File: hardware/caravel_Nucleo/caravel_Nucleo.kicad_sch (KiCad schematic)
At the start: 82 parts, among them J1 USB4105-GF-A, J10 PinHeader_1x11, J11 PinHeader_1x02, J12 PinHeader_1x02, J3 PinHeader_1x02, J4 836-22-004-10-001101, J5 PinHeader_1x02, J6 PinHeader_1x02, J7 836-22-006-10-001101, J8 640456-3, J9 640456-3, SW1 KMR2, T1 Logo, T2 Logo, U1 FT232HQ, U12 NUCLEO144-F429ZI, U2 SN74LVC1G125DCKR, U3 SN74LVC1G125DCKR, U4 MAX811REUS+T, U7 W25Q32FVSS, U8 caravel_breakout, U9 MIC2211-AAYML-TR, X1 ECS-2520MVLC-100-BN-TR, Y1 ABM8G-12.000MHZ-18-D2Y-T

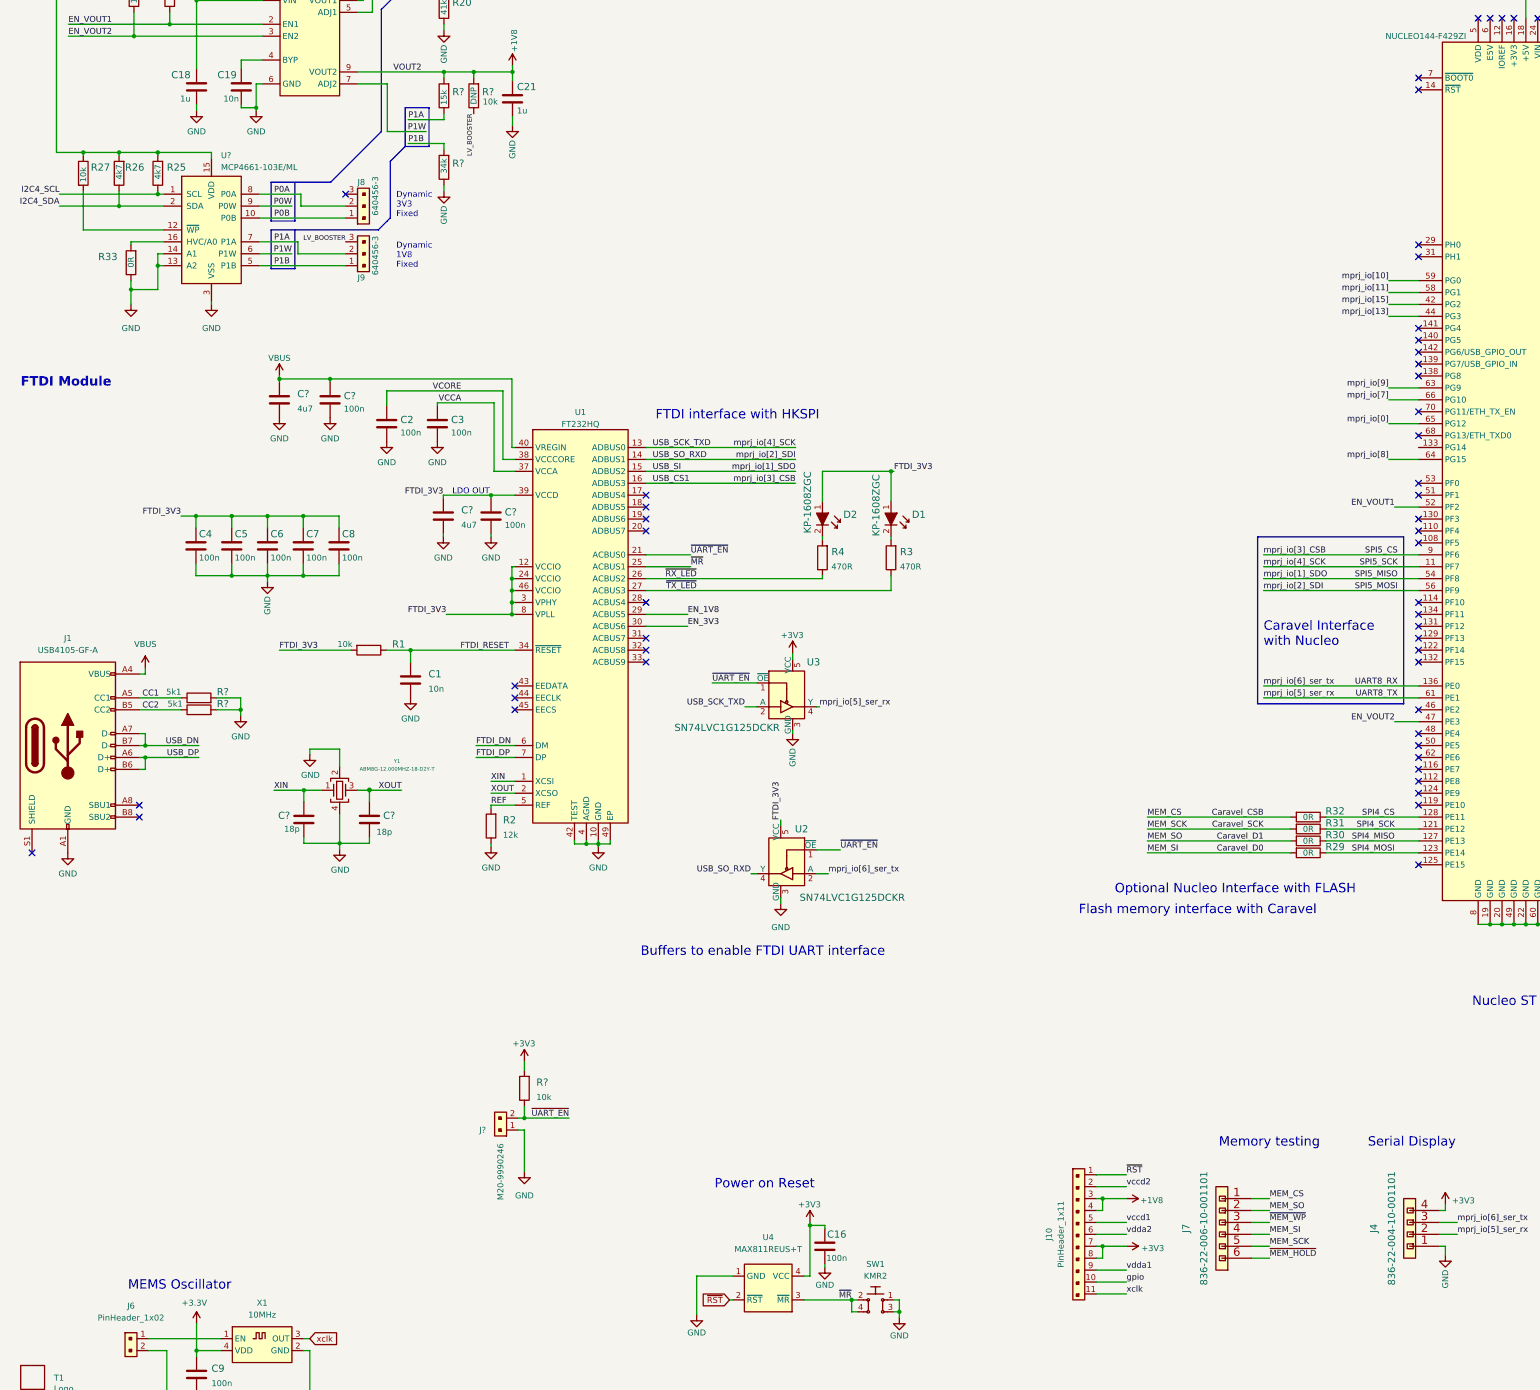
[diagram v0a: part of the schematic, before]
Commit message: Annotate parts on schematic
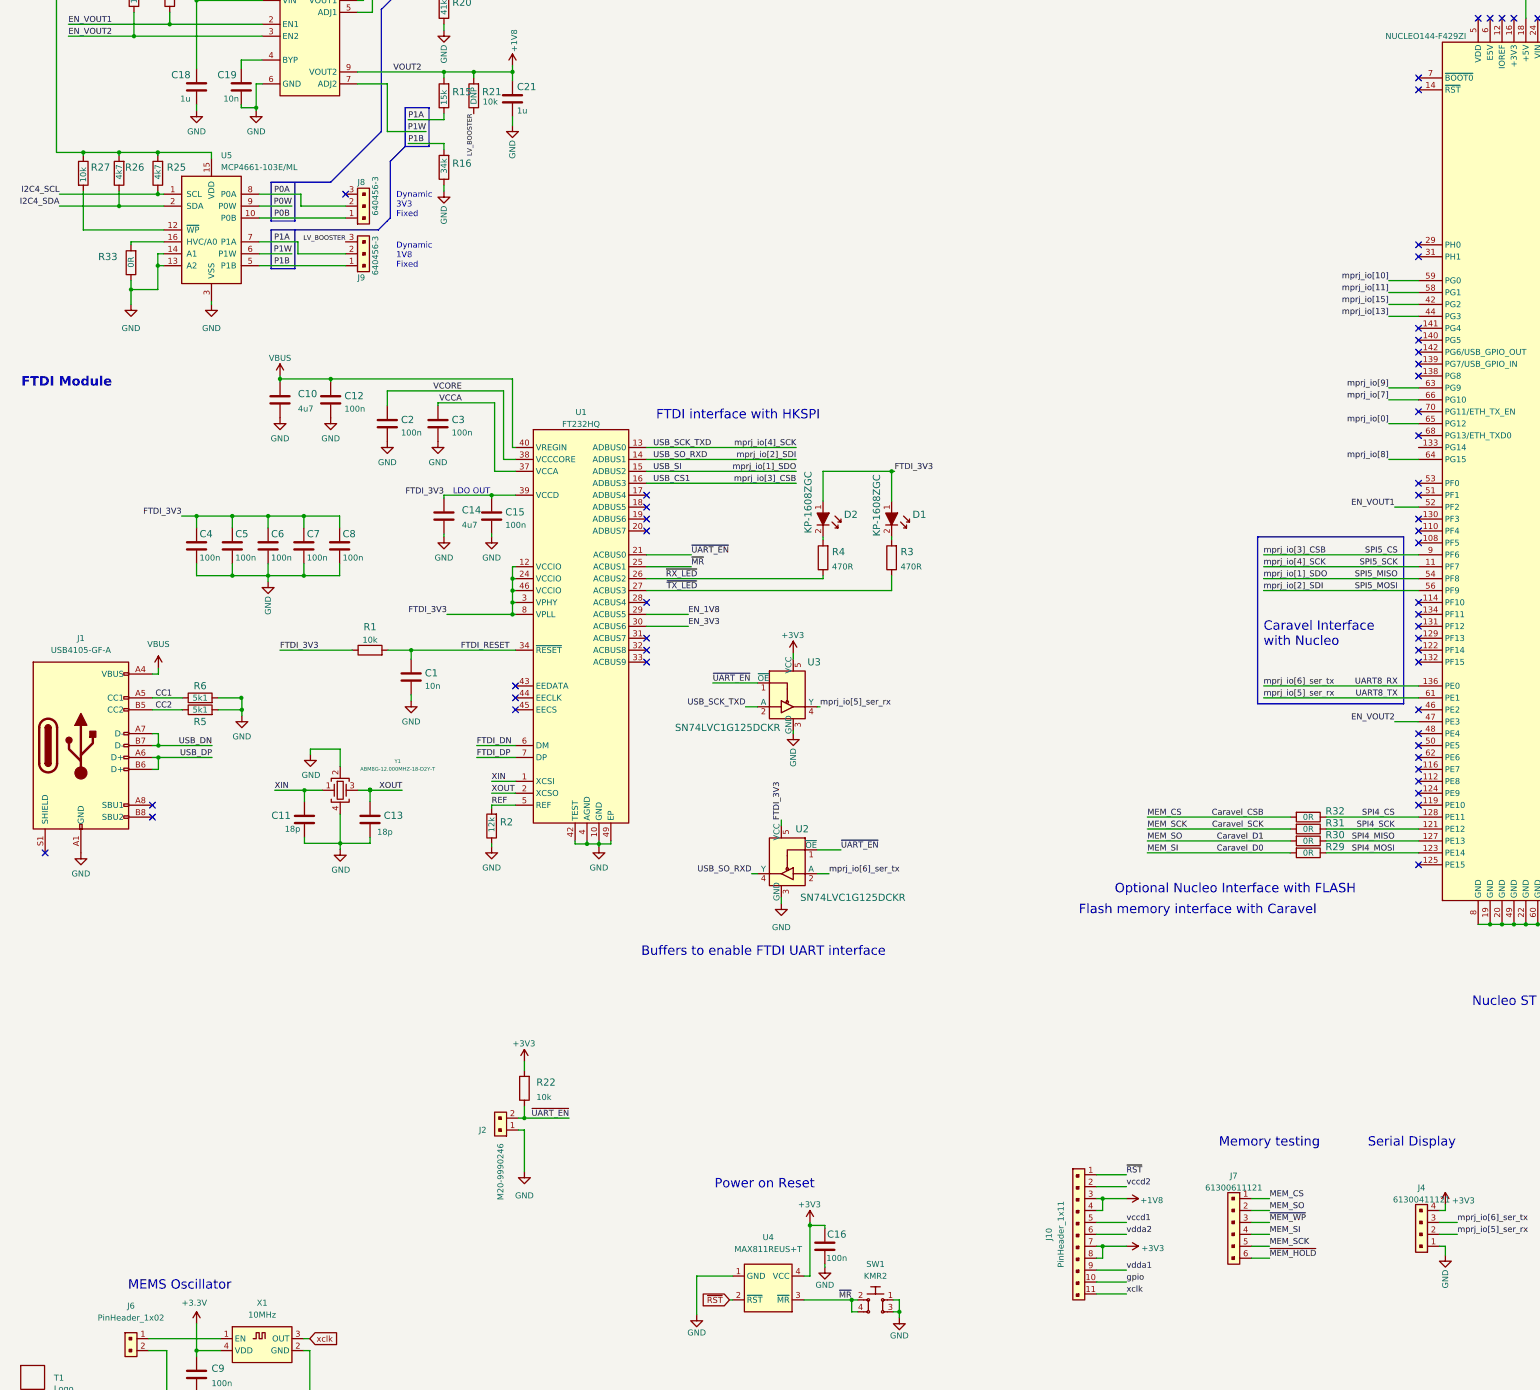
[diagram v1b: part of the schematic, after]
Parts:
- removed C1: C_10n_0402, antmicro-footprints:0402-cap, symbol antmicroCapacitors0402:C_10n_0402
- removed J4: 836-22-004-10-001101, antmicro-footprints:PogoPinHeader_1x4_P2mm_Drill1,5mm, symbol antmicroRectangularConnectorsHeadersMalePins:836-22-004-10-001101
- removed J7: 836-22-006-10-001101, antmicro-footprints:PogoPinHeader_1x6_P2mm_Drill1,5mm, symbol antmicroRectangularConnectorsHeadersMalePins:836-22-006-10-001101
- removed R1: R_10k_0402, antmicro-footprints:0402-res, symbol antmicroResistors0402:R_10k_0402
- removed R2: R_12k_0402, antmicro-footprints:0402-res, symbol antmicroResistors0402:R_12k_0402
- removed R? (x2): R_5k1_0402, antmicro-footprints:0402-res, symbol antmicroResistors0402:R_5k1_0402
- added C1: C_10n_0603, antmicro-footprints:0603-cap, symbol antmicroCapacitors0603:C_10n_0603
- added J4: 61300411121, antmicro-footprints:PinHeader_1x4_P2.54mm_Drill1.02mm, symbol antmicroRectangularConnectorsHeadersMalePins:61300411121
- added J7: 61300611121, antmicro-footprints:61300611121, symbol antmicroRectangularConnectorsHeadersMalePins:61300611121
- added R1: R_10k_0603, antmicro-footprints:0603-res, symbol antmicroResistors0603:R_10k_0603
- added R2: R_12k_0603, antmicro-footprints:0603-res, symbol antmicroResistors0603:R_12k_0603
- added R5, R6: R_5k1_0603, antmicro-footprints:0603-res, symbol antmicroResistors0603:R_5k1_0603
- T1: footprint Caravel_Board:logo -> antmicro-footprints:efabless_logo_2
- T2: footprint Caravel_Board:ef_logo -> antmicro-footprints:efabless_logo
- gave numbers to parts that had none: 12
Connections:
- net +3V3: now also J4.4
- net AGND: now also C1.2, J4.1, R2.1, R5.2, R6.2
- net CC1: now also R6.1
- net CC2: now also R5.1
- net Caravel_CSB: now also J7.1
- net Caravel_D0: now also J7.4
- net Caravel_D1: now also J7.2
- net Caravel_SCK: now also J7.5
- net FTDI_3V3: now also R1.1
- net FTDI_RESET: now also C1.1, R1.2
- net REF: now also R2.2
- net UART8_RX: now also J4.3
- net UART8_TX: now also J4.2
- net ~{MEM_HOLD}: now also J7.6
- net ~{MEM_WP}: now also J7.3
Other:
- moved on the sheet: J1

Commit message: Further connection tidy up, regroup components in to logical blocks, add gpio LED PMOS, add possiblility to supply device with USB VBUS
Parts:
- removed U8: caravel_breakout, antmicro-footprints:caravel_breakout, symbol antmicroModules:caravel_breakout
- added C? (x2): C_100n_0603, antmicro-footprints:0603-cap, symbol antmicroCapacitors0603:C_100n_0603
- added D? (x2): 1N5819HW-7-F, antmicro-footprints:SOD-123, symbol antmicroDiodesRectifiersSingle:1N5819HW-7-F
- added Q?: BSS84AKW, antmicro-footprints:SOT-323, symbol antmicroTransistorsFETsMOSFETsSingle:BSS84AKW
- added R?: R_10k_0402, antmicro-footprints:0402-res, symbol antmicroResistors0402:R_10k_0402
- added U?: Caravel_breakout_PCB, antmicro-footprints:caravel_breakout, symbol antmicroModules:Caravel_breakout_PCB
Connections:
- net USB_DN is gone; now on net FTDI_DN: J1.A7 (D-), J1.B7 (D-)
- net USB_DP is gone; now on net FTDI_DP: J1.A6 (D+), J1.B6 (D+)
- net +1V8: now also U?.43 (VCCD1), U?.50 (VCCD), U?.6 (VCCD)
- net +3V3: now also C?.1, C?.1, Q?.2 (S), U?.45 (VDDA), U?.55 (VDDIO), U?.7 (VDDIO); no longer R13.2
- net AGND: now also D3.2, C?.2, C?.2, U?.5 (GND), U?.8 (GND)
- net Caravel_CSB: now also U?.51 (~{FLASH_CS})
- net Caravel_D0: now also U?.49 (FLASH_D0)
- net Caravel_D1: now also U?.48 (FLASH_D1)
- net Caravel_SCK: now also U?.46 (FLASH_SCK)
- net FTDI_3V3: no longer U1.12 (VCCIO), U1.24 (VCCIO), U1.3 (VPHY), U1.46 (VCCIO), U1.8 (VPLL)
- net NU_5V: now also D?.A; no longer C18.1, R17.2, R18.2, R25.2, R26.2, R27.1, U5.15 (VDD), U9.1 (VIN)
- net SPI5_CS: now also U?.39 (~{CS}_IO3)
- net SPI5_MISO: now also U?.41 (SDO_IO1)
- net SPI5_MOSI: now also U?.40 (SDI_IO2)
- net SPI5_SCK: now also U?.38 (SCK_IO4)
- net UART8_RX: now also U?.36 (TX_IO6)
- net UART8_TX: now also U?.37 (RX_IO5)
- net VBUS: now also D?.A
- net gpio: now also R?.2, U?.47 (GPIO); no longer D3.2
- net mprj_io[0]: now also U?.42 (IO0)
- net mprj_io[10]: now also U?.32 (IO10)
- net mprj_io[11]: now also U?.31 (IO11)
- net mprj_io[12]: now also U?.30 (IO12)
- net mprj_io[13]: now also U?.29 (IO13)
- net mprj_io[14]: now also U?.28 (IO14)
- net mprj_io[15]: now also U?.27 (IO15)
- net mprj_io[16]: now also U?.26 (IO16)
- net mprj_io[17]: now also U?.25 (IO17)
- net mprj_io[18]: now also U?.24 (IO18)
- net mprj_io[19]: now also U?.23 (IO19)
- net mprj_io[20]: now also U?.22 (IO20)
- net mprj_io[21]: now also U?.21 (IO21)
- net mprj_io[22]: now also U?.20 (IO22)
- net mprj_io[23]: now also U?.19 (IO23)
- net mprj_io[24]: now also U?.18 (IO24)
- net mprj_io[25]: now also U?.17 (IO25)
- net mprj_io[26]: now also U?.16 (IO26)
- net mprj_io[27]: now also U?.15 (IO27)
- net mprj_io[28]: now also U?.14 (IO28)
- net mprj_io[29]: now also U?.13 (IO29)
- net mprj_io[30]: now also U?.12 (IO30)
- net mprj_io[31]: now also U?.11 (IO31)
- net mprj_io[32]: now also U?.10 (IO32)
- net mprj_io[33]: now also U?.9 (IO33)
- net mprj_io[34]: now also U?.4 (IO34)
- net mprj_io[35]: now also U?.3 (IO35)
- net mprj_io[36]: now also U?.2 (IO36)
- net mprj_io[37]: now also U?.1 (IO37)
- net mprj_io[7]: now also U?.35 (IO7)
- net mprj_io[8]: now also U?.34 (IO8)
- net mprj_io[9]: now also U?.33 (IO9)
- net vccd2: now also U?.56 (VCCD2)
- net vdda1: now also U?.44 (VDDA1)
- net vdda2: now also U?.54 (VDDA2)
- net xclk: now also U?.52 (XCLK)
- net ~{RST}: now also U?.53 (~{RST})
- new net: C18.1, D?.K, D?.K, R17.2, R18.2, R25.2, R26.2, R27.1, U5.15 (VDD), U9.1 (VIN)
- new net: Q?.1 (G), R?.1
- new net: U1.12 (VCCIO), U1.24 (VCCIO), U1.3 (VPHY), U1.46 (VCCIO), U1.8 (VPLL)
- new net: Q?.3 (D), R13.2
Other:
- note added: "- LDO EN? - vccd2 unconnected?"
- note added: "Caravel"
- note added: "Connectors"
- note added: "Mechanical"
- note added: "Nucleo ST Morpho Connector"
- note added: "Supply"
- note added: "To clarify: -FTDI dual function and UART buffering (FTDI2232 ?) -Minimum VCCD supply level (LV_BOOSTER) -Shorting ~{UART_EN} by J2"
- moved on the sheet: C1, C10, C11, C12, C13, C14, C15, C16, C17, C18, C19, C2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

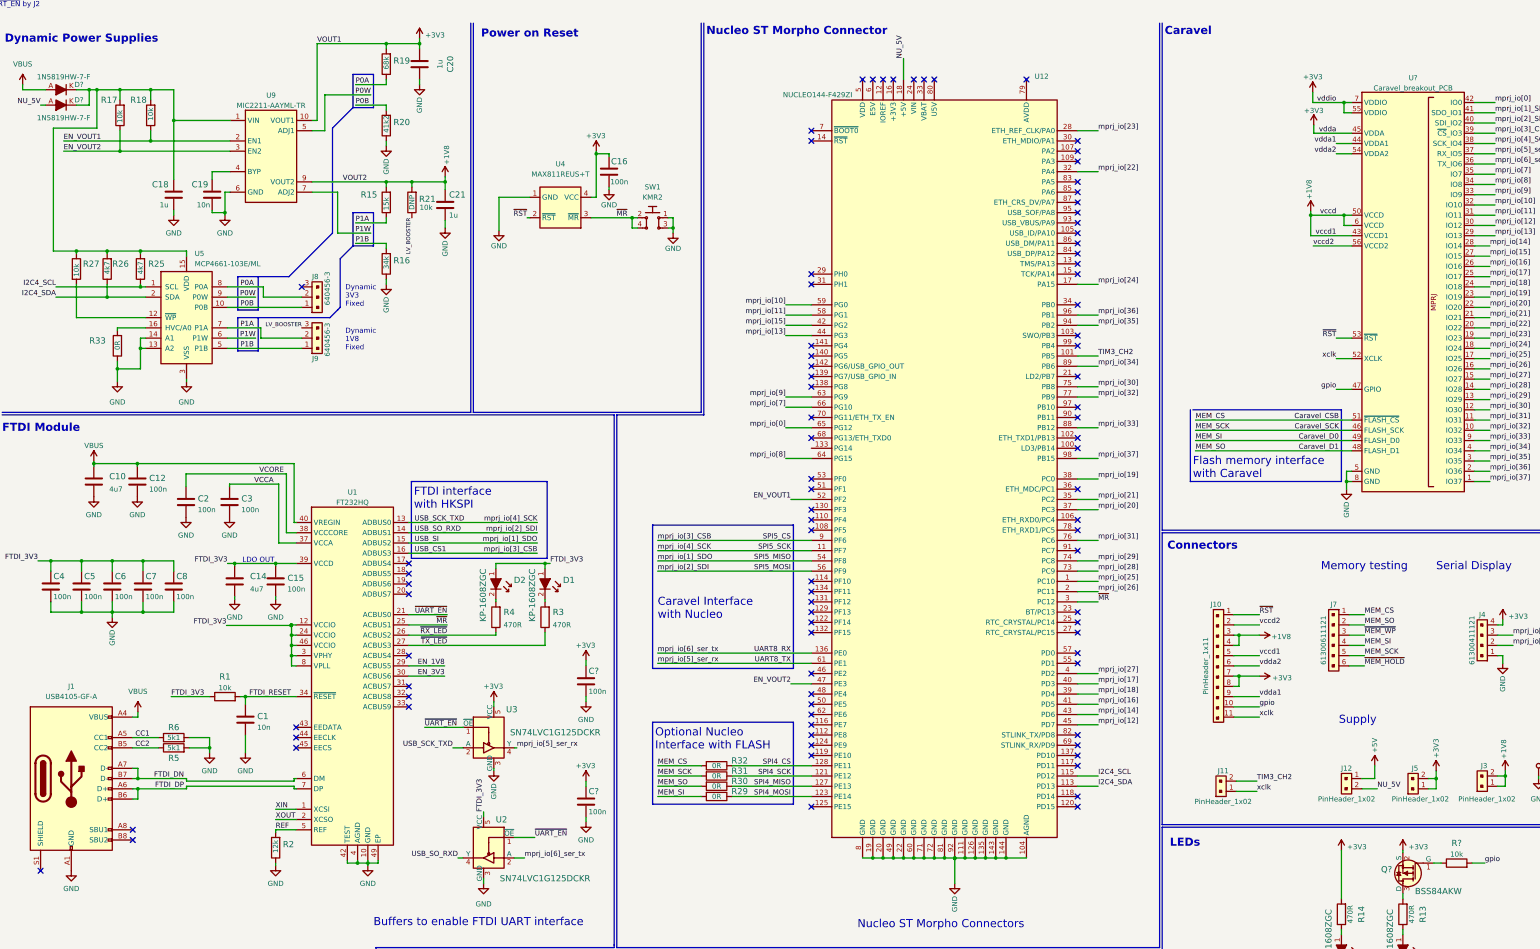
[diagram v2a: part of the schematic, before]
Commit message: Update FTDI symbol
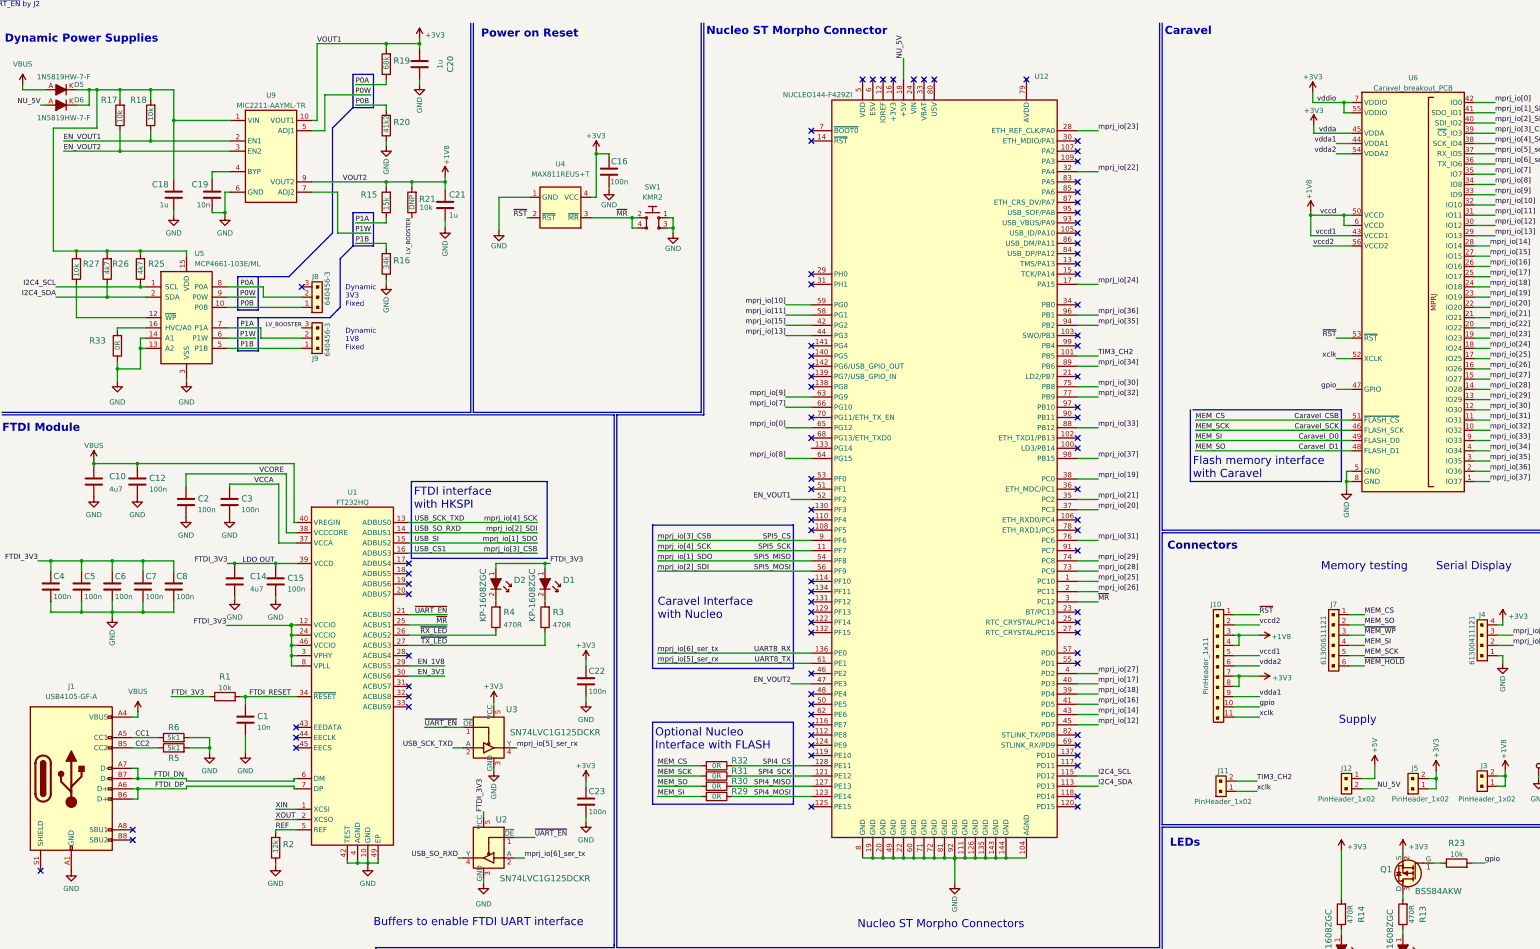
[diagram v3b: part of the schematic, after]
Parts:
- U1: footprint antmicro-footprints:QFN-48-1EP_6x6mm -> antmicro-footprints:QFN-48-1EP_8x8mm_P0.5mm_EP6.2x6.2mm_FT232HQ_marking
- gave numbers to parts that had none: 7
